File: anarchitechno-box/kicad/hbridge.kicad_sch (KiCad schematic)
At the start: 16 parts, among them U11 DRV8243SQDGQRQ1

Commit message: Stijn in de Trein
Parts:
- D6: footprint LED_SMD:LED_0805_2012Metric -> LED_SMD:LED_0603_1608Metric
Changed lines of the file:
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@@
 			)
 		)
-		(property "Footprint" "LED_SMD:LED_0805_2012Metric"
+		(property "Footprint" "LED_SMD:LED_0603_1608Metric"
 			(at 111.76 63.5 0)
 			(effects

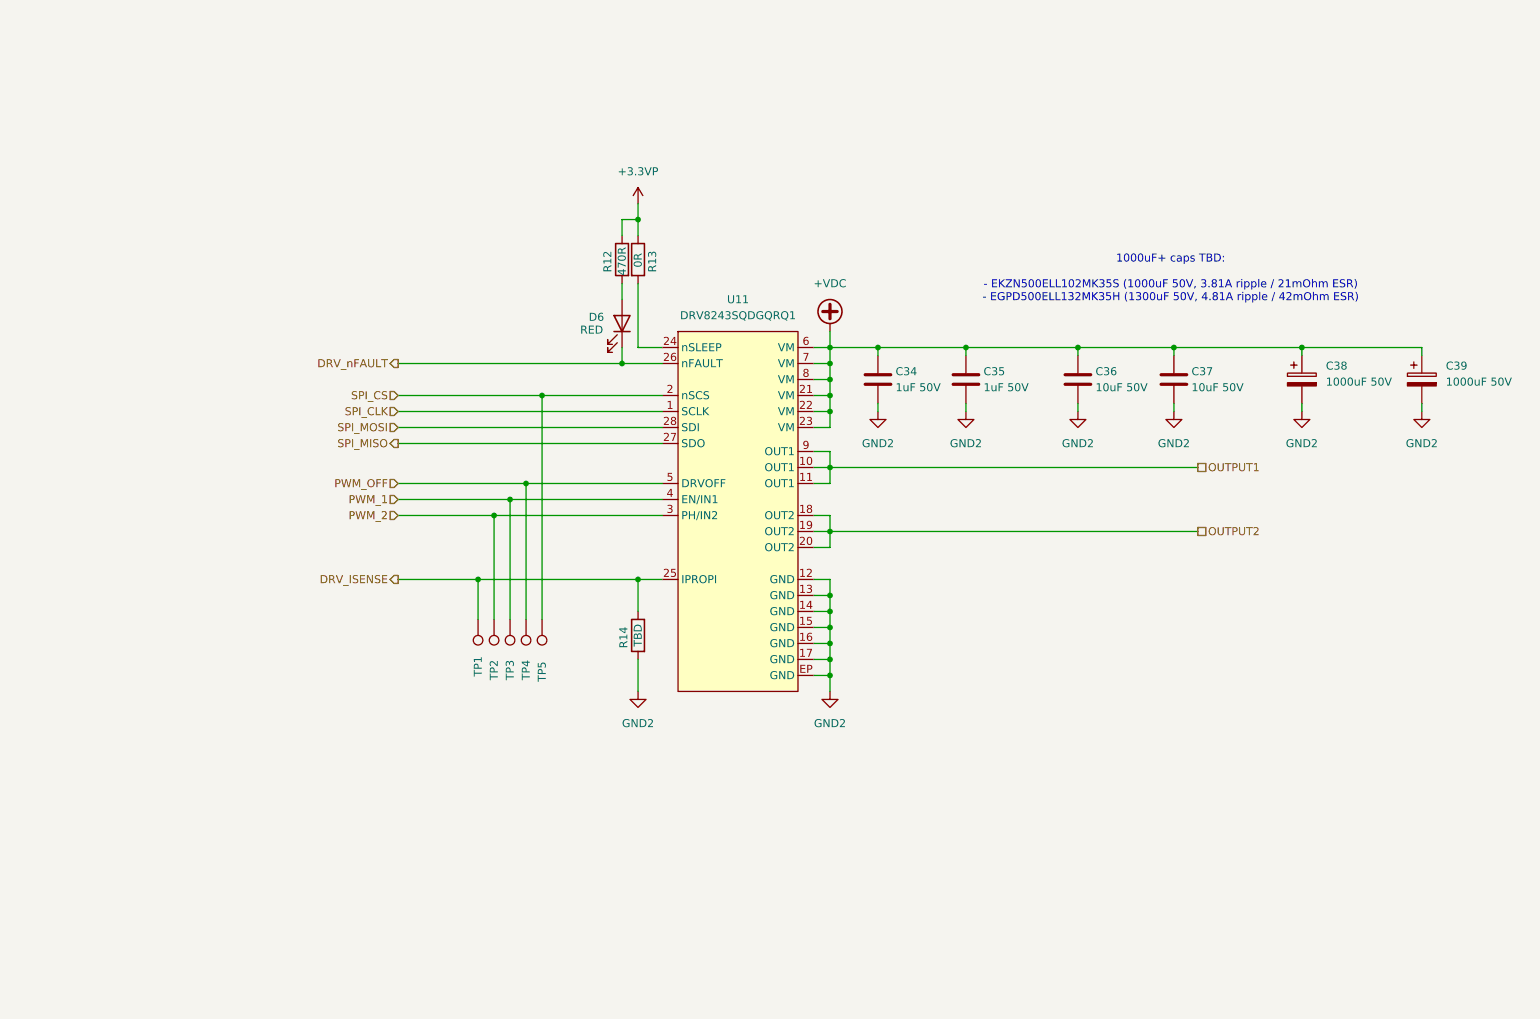
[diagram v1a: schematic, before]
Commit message: IPROPI comments on H-bridge
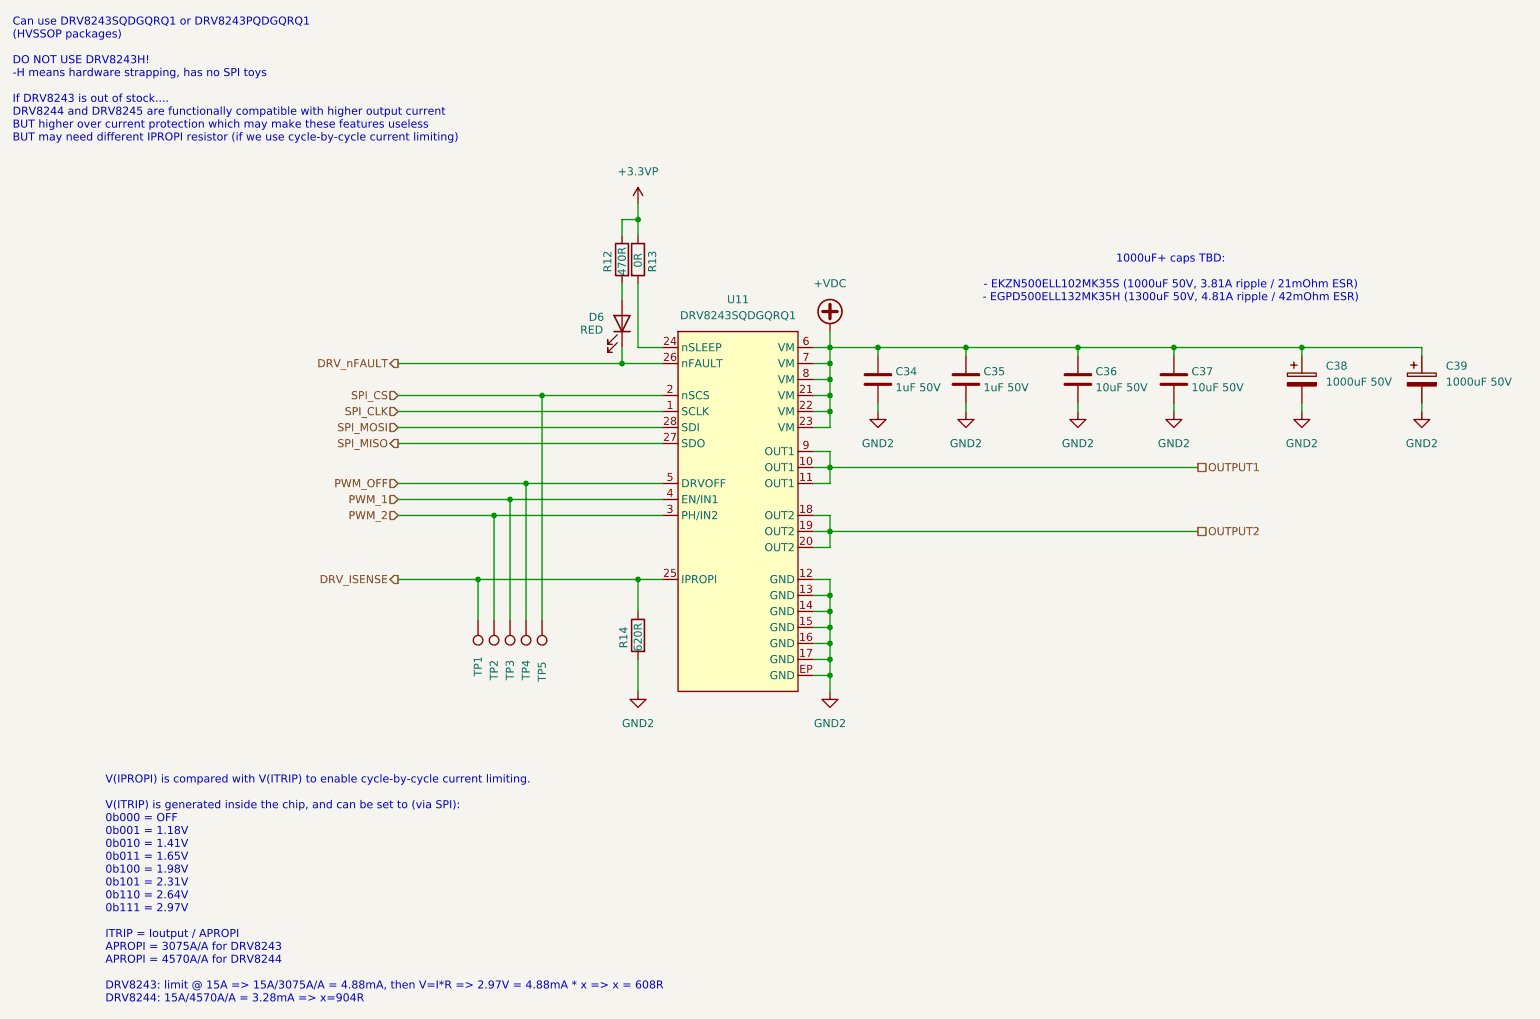
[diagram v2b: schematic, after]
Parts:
- R14: value TBD -> 620R
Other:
- note added: "Can use DRV8243SQDGQRQ1 or DRV8243PQDGQRQ1 (HVSSOP packages) DO NOT USE DRV8243H! -H means hardware strapping, has no SPI toys If DRV8243 is out of stock.... DRV8244 and DRV8245 are functionally compatible with higher output current BUT higher over current protection which may make these features useless BUT may need different IPROPI resistor (if we use cycle-by-cycle current limiting)"
- note added: "V(IPROPI) is compared with V(ITRIP) to enable cycle-by-cycle current limiting. V(ITRIP) is generated inside the chip, and can be set to (via SPI): 0b000 = OFF 0b001 = 1.18V 0b010 = 1.41V 0b011 = 1.65V 0b100 = 1.98V 0b101 = 2.31V 0b110 = 2.64V 0b111 = 2.97V ITRIP = Ioutput / APROPI APROPI = 3075A/A for DRV8243 APROPI = 4570A/A for DRV8244 DRV8243: limit @ 15A => 15A/3075A/A = 4.88mA, then V=I*R =>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"
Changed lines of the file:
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@@
 	(generator_version "9.0")
 	(paper "A4")
+	(text "Can use DRV8243SQDGQRQ1 or DRV8243PQDGQRQ1\n(HVSSOP packages)\n\nDO NOT USE DRV8243H!\n-H means hardware strapping, has no SPI toys\n\nIf DRV8243 is out of stock....\nDRV8244 and DRV8245 are functionally compatible with higher output current\nBUT higher over current protection which may make these features useless\nBUT may need different IPROPI resistor (if we use cycle-by-cycle current limiting)"
+		(exclude_from_sim no)
+		(at 14.986 24.892 0)
+		(effects
+			(font
+				(size 1.27 1.27)
+			)
+			(justify left)
+		)
+	)
 	(text "1000uF+ caps TBD:\n\n- EKZN500ELL102MK35S (1000uF 50V, 3.81A ripple / 21mOhm ESR)\n- EGPD500ELL132MK35H (1300uF 50V, 4.81A ripple / 42mOhm ESR)"
 		(exclude_from_sim no)
@@
 				(size 1.27 1.27)
 			)
+		)
+	)
+	(text "V(IPROPI) is compared with V(ITRIP) to enable cycle-by-cycle current limiting.\n\nV(ITRIP) is generated inside the chip, and can be set to (via SPI):\n0b000 = OFF\n0b001 = 1.18V\n0b010 = 1.41V\n0b011 = 1.65V\n0b100 = 1.98V\n0b101 = 2.31V\n0b110 = 2.64V\n0b111 = 2.97V\n\nITRIP = Ioutput / APROPI\nAPROPI = 3075A/A for DRV8243\nAPROPI = 4570A/A for DRV8244\n\nDRV8243: limit @ 15A => 15A/3075A/A = 4.88mA, then V=I*R => 2.97V = 4.88mA * x => x = 608R\nDRV8244: 15A/4570A/A = 3.28mA => x=904R"
+		(exclude_from_sim no)
+		(at 29.718 153.416 0)
+		(effects
+			(font
+				(size 1.27 1.27)
+			)
+			(justify left)
 		)
 	)
@@
 			)
 		)
-		(property "Value" "TBD"
-			(at 114.3 114.808 90)
-			(effects
-				(font
+		(property "Value" "620R"
+			(at 114.3 115.57 90)
+			(effects
+				(font

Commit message: Resized PCB with mounts at 125x125mm (suitable for 140mm PC fan), 4-pin fan connector added, changed 3.3VP to 5.0VP
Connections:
- net +3.3VP renamed +5VP
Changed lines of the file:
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@@
-	)
-	(symbol
-		(lib_id "power:+3.3VP")
-		(at 114.3 44.45 0)
-		(unit 1)
-		(exclude_from_sim no)
-		(in_bom yes)
-		(on_board yes)
-		(dnp no)
-		(fields_autoplaced yes)
-		(property "Reference" "#PWR069"
-			(at 118.11 45.72 0)
-			(effects
-				(font
-					(size 1.27 1.27)
-				)
-				(hide yes)
-			)
-		)
-		(property "Value" "+3.3VP"
-			(at 114.3 39.37 0)
-			(effects
-				(font
-					(size 1.27 1.27)
-				)
-			)
-		)
-		(property "Footprint" ""
-			(at 114.3 44.45 0)
-			(effects
-				(font
-					(size 1.27 1.27)
-				)
-				(hide yes)
-			)
-		)
-		(property "Datasheet" ""
-			(at 114.3 44.45 0)
-			(effects
-				(font
-					(size 1.27 1.27)
-				)
-				(hide yes)
-			)
-		)
-		(property "Description" "Power symbol creates a global label with name \"+3.3VP\""
-			(at 114.3 44.45 0)
-			(effects
-				(font
-					(size 1.27 1.27)
-				)
-				(hide yes)
-			)
-		)
-		(pin "1"
-		)
-		(instances
-			(project "anarchytechnobox"
-				(path "/8c734c41-38ed-40fc-83bd-134786dcfb35/48f260d8-d62f-49a9-8985-05fca65ac6cb/0c0607e4-80d3-46ba-8adb-76563a900b03"
-					(reference "#PWR0145")
-					(unit 1)
-				)
-				(path "/8c734c41-38ed-40fc-83bd-134786dcfb35/48f260d8-d62f-49a9-8985-05fca65ac6cb/ec360df5-fff7-49b0-afa3-93c9754653a9"
-					(reference "#PWR0135")
-					(unit 1)
-				)
-				(path "/8c734c41-38ed-40fc-83bd-134786dcfb35/f97c65ed-bb3f-4eb8-a2c6-056cc510b5f8/0c0607e4-80d3-46ba-8adb-76563a900b03"
-					(reference "#PWR079")
-					(unit 1)
-				)
-				(path "/8c734c41-38ed-40fc-83bd-134786dcfb35/f97c65ed-bb3f-4eb8-a2c6-056cc510b5f8/ec360df5-fff7-49b0-afa3-93c9754653a9"
-					(reference "#PWR069")
-					(unit 1)
-				)
-			)
-		)
 	)
 	(symbol
@@
 					(unit 1)
 				)
+			)
+		)
+	)
+	(symbol
+		(lib_id "power:+5VP")
+		(at 114.3 44.45 0)
+		(unit 1)
+		(exclude_from_sim no)
+		(in_bom yes)
+		(on_board yes)
+		(dnp no)
+		(fields_autoplaced yes)
+		(property "Reference" "#PWR059"
+			(at 114.3 48.26 0)
+			(effects
+				(font
+					(size 1.27 1.27)
+				)
+				(hide yes)
+			)
+		)
+		(property "Value" "+5VP"
+			(at 114.3 39.37 0)
+			(effects
+				(font
+					(size 1.27 1.27)
+				)
+			)
+		)
+		(property "Footprint" ""
+			(at 114.3 44.45 0)
+			(effects
+				(font
+					(size 1.27 1.27)
+				)
+				(hide yes)
+			)
+		)
+		(property "Datasheet" ""
+			(at 114.3 44.45 0)
+			(effects
+				(font
+					(size 1.27 1.27)
+				)
+				(hide yes)
+			)
+		)
+		(property "Description" "Power symbol creates a global label with name \"+5VP\""
+			(at 114.3 44.45 0)
+			(effects
+				(font
+					(size 1.27 1.27)
+				)
+				(hide yes)
+			)
+		)
+		(pin "1"
+		)
+		(instances
+			(project "anarchytechnobox"
+				(path "/8c734c41-38ed-40fc-83bd-134786dcfb35/48f260d8-d62f-49a9-8985-05fca65ac6cb/0c0607e4-80d3-46ba-8adb-76563a900b03"
+					(reference "#PWR069")
+					(unit 1)
+				)
+				(path "/8c734c41-38ed-40fc-83bd-134786dcfb35/48f260d8-d62f-49a9-8985-05fca65ac6cb/ec360df5-fff7-49b0-afa3-93c9754653a9"
+					(reference "#PWR067")
+					(unit 1)
+				)
+				(path "/8c734c41-38ed-40fc-83bd-134786dcfb35/f97c65ed-bb3f-4eb8-a2c6-056cc510b5f8/0c0607e4-80d3-46ba-8adb-76563a900b03"
+					(reference "#PWR065")
+					(unit 1)
+				)
+				(path "/8c734c41-38ed-40fc-83bd-134786dcfb35/f97c65ed-bb3f-4eb8-a2c6-056cc510b5f8/ec360df5-fff7-49b0-afa3-93c9754653a9"
+					(reference "#PWR059")
+					(unit 1)
+				)
